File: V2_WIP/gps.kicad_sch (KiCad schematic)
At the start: 38 parts, among them J4 BATT, SW1 RotaryEncoder, SW2 MSN22AFW01, U10 24C32, U101 DFR0654, U2 TPS613222ADBVR

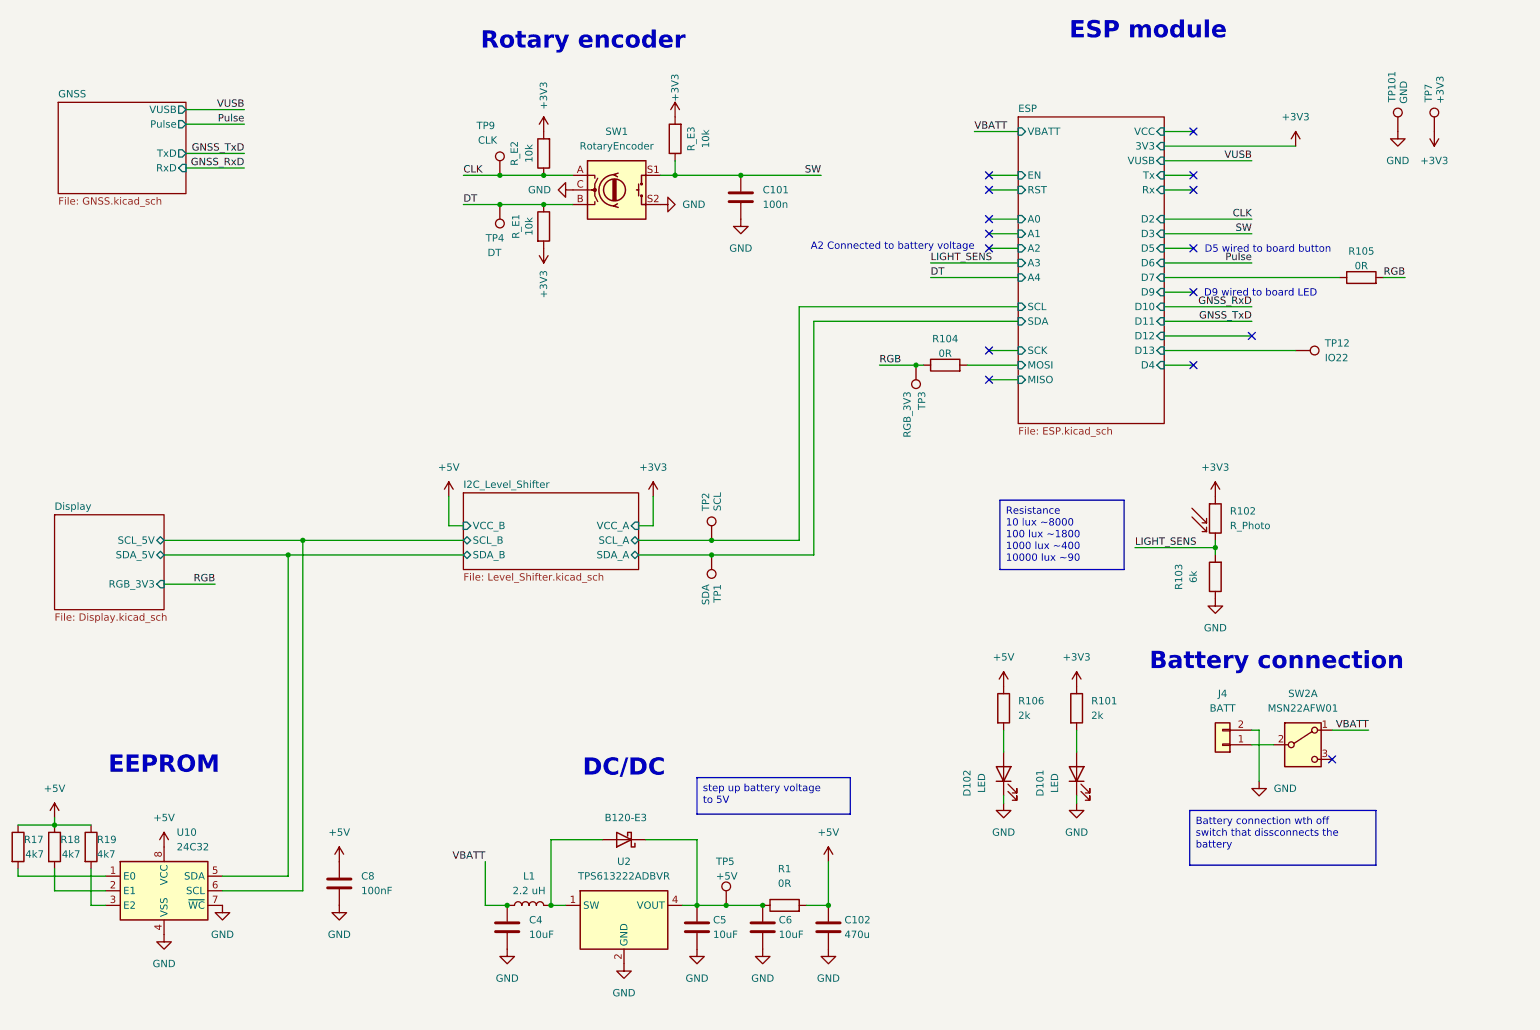
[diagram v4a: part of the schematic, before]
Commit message: added battery monitoring circuits
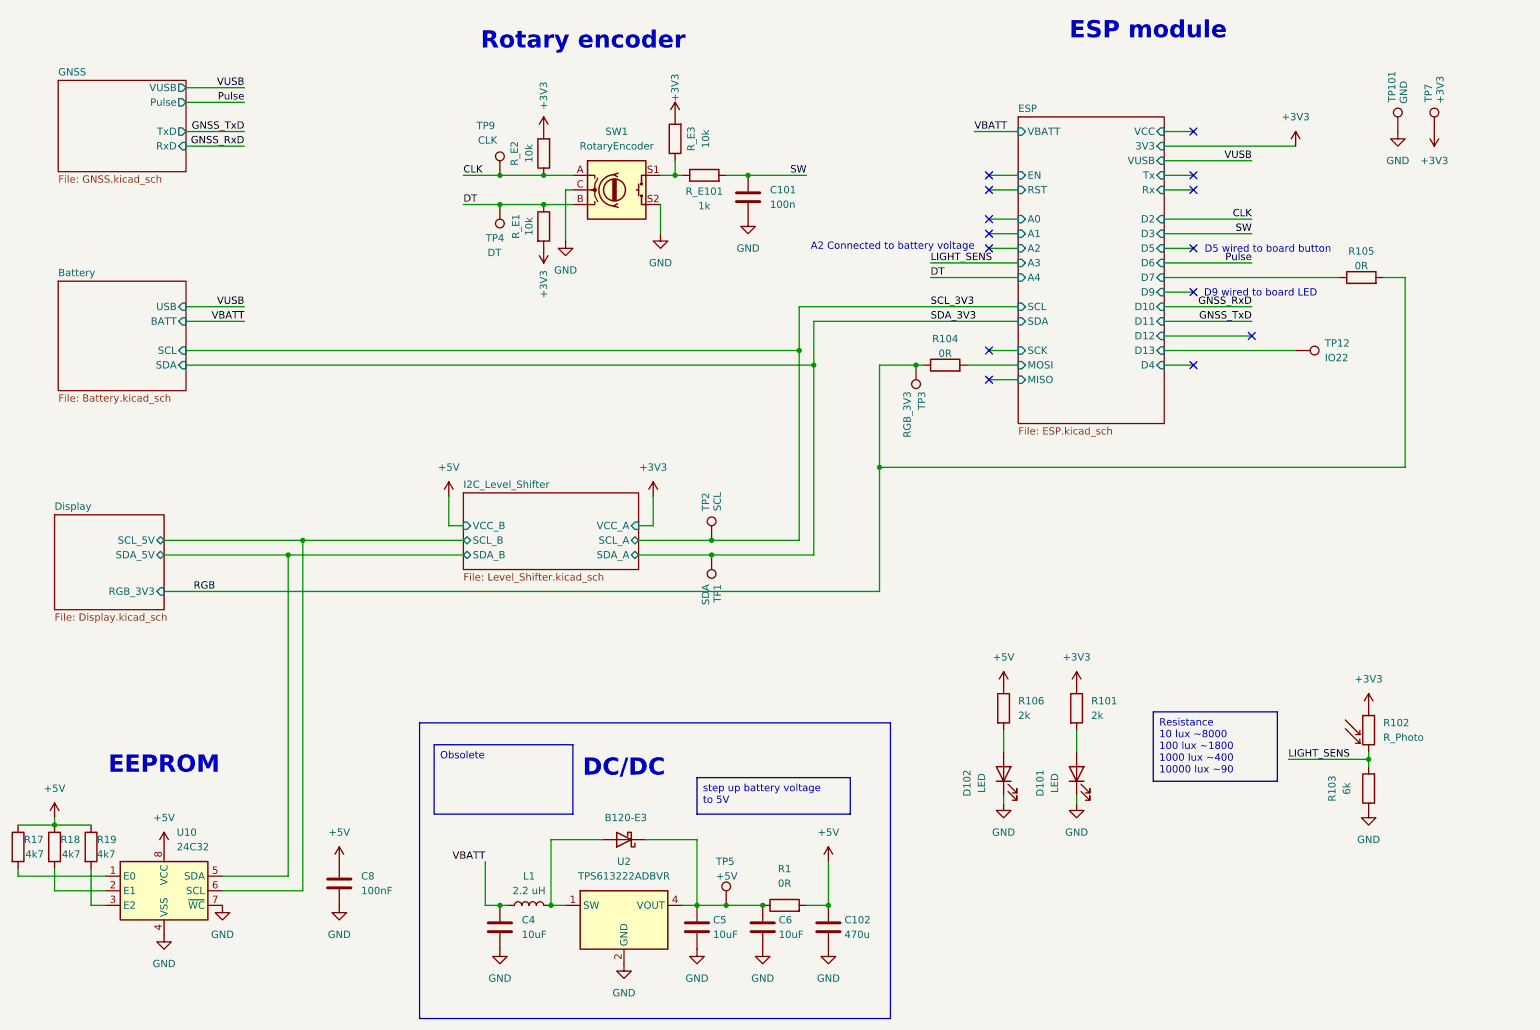
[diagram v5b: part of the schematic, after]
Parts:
- removed J4: BATT, 1769:1769, symbol Connector_Generic:Conn_01x02
- removed SW2: MSN22AFW01, Button_Switch_THT:MSN22AFW01, symbol Switch:SW_DPDT_x2
- added R_E101: 1k, Resistor_SMD:R_0805_2012Metric_Pad1.20x1.40mm_HandSolder, symbol Device:R
- D101, D102: footprint LED_THT:LED_D3.0mm -> Diode_SMD:D_0603_1608Metric_Pad1.05x0.95mm_HandSolder
- R104, R105: footprint Resistor_SMD:R_0805_2012Metric_Pad1.20x1.40mm_HandSolder -> Resistor_SMD:R_0603_1608Metric_Pad0.98x0.95mm_HandSolder
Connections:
- net SW: now also R_E101.2; no longer R_E3.1, SW1.S1
- net ESP/SCL renamed SCL_3V3
- net ESP/SDA renamed SDA_3V3
- new net: R_E101.1, R_E3.1, SW1.S1
- no-connect marks 15 -> 14
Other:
- added sheet Battery (Battery.kicad_sch)
- note removed: "Battery connection"
- moved on the sheet: C101, C4, R102, R103

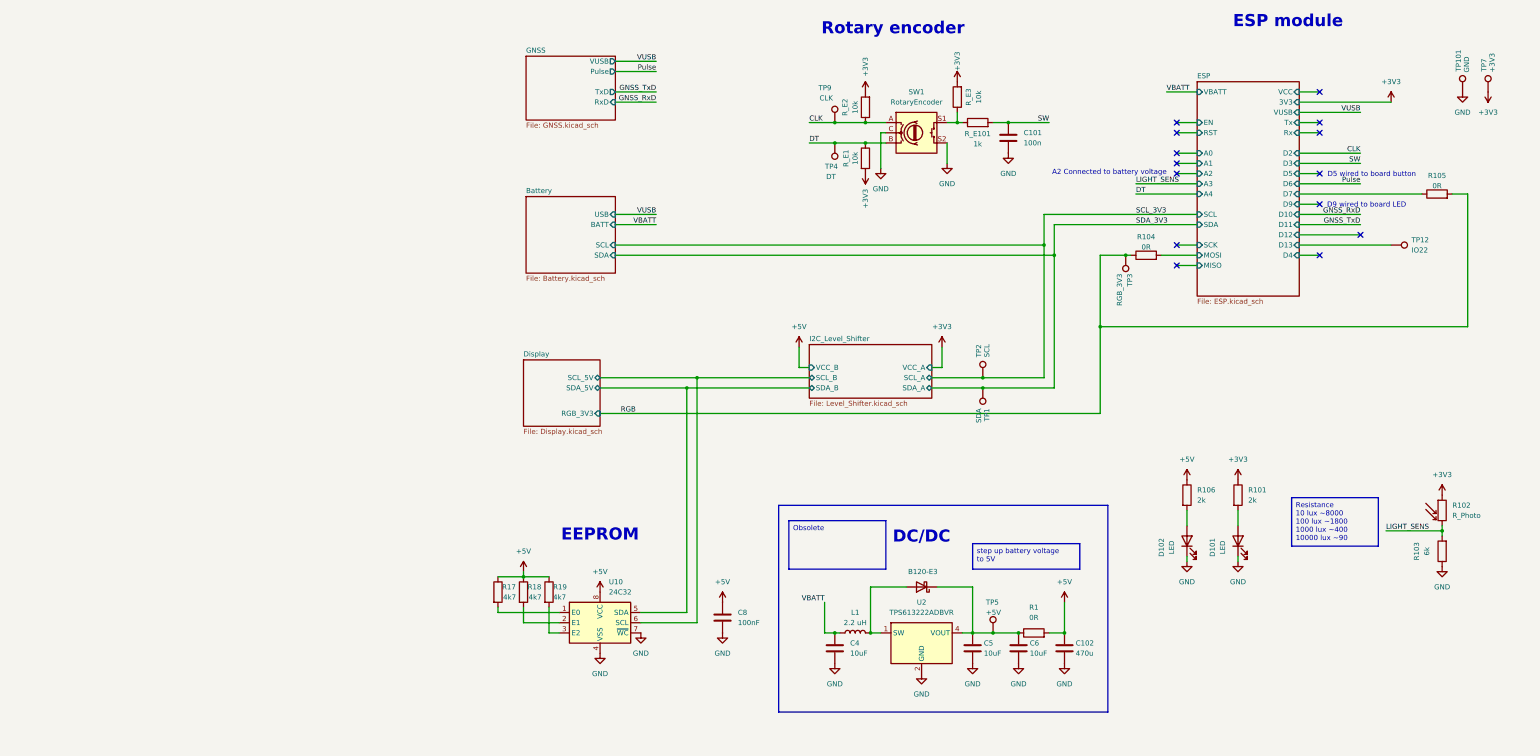
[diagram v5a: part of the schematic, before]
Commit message: added FLASH module; moved encoder into separate schematic
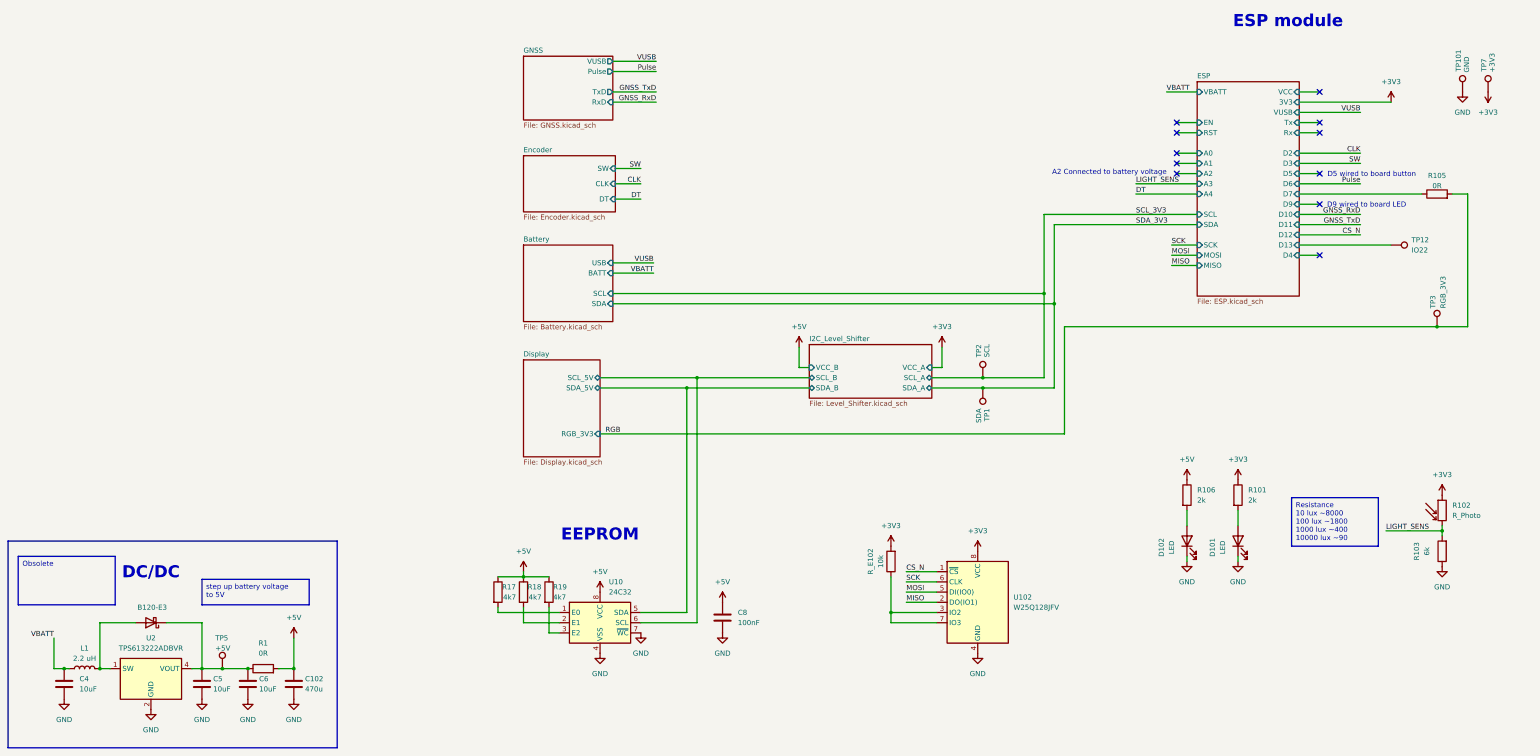
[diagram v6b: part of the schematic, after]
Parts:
- removed C101: 100n, Capacitor_SMD:C_0603_1608Metric_Pad1.08x0.95mm_HandSolder, symbol Device:C
- removed R104: 0R, Resistor_SMD:R_0603_1608Metric_Pad0.98x0.95mm_HandSolder, symbol Device:R
- removed R_E1, R_E2, R_E3: 10k, Resistor_SMD:R_0805_2012Metric_Pad1.20x1.40mm_HandSolder, symbol Device:R
- removed R_E101: 1k, Resistor_SMD:R_0805_2012Metric_Pad1.20x1.40mm_HandSolder, symbol Device:R
- removed SW1: RotaryEncoder, Rotary_Encoder:RotaryEncoder_Alps_EC12E-Switch_Vertical_H20mm_CircularMountingHoles, symbol Device:RotaryEncoder_Switch
- removed TP4: DT, TestPoint:TestPoint_Pad_D1.5mm, symbol Connector:TestPoint
- removed TP9: CLK, TestPoint:TestPoint_Pad_D1.5mm, symbol Connector:TestPoint
- added R_E102: 10k, Resistor_SMD:R_0805_2012Metric_Pad1.20x1.40mm_HandSolder, symbol Device:R
- added U102: W25Q128JFV, Package_SO:SOIC-8_5.23x5.23mm_P1.27mm, symbol Memory_Flash:W25Q128JVS
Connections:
- net +3V3: now also R_E102.2, U102.8 (VCC)
- net GND: now also U102.4 (GND)
- new net: R_E102.1, U102.3 (IO2), U102.7 (IO3)
- new net CS_N: U102.1 (~{CS})
- new net MISO: U102.2 (DO(IO1))
- new net MOSI: U102.5 (DI(IO0))
- new net SCK: U102.6 (CLK)
- no-connect marks 14 -> 11
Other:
- added sheet Encoder (Encoder.kicad_sch)
- note removed: "Rotary encoder"
- moved on the sheet: C102, C4, C5, C6, L1, R1, TP3, TP5, U2

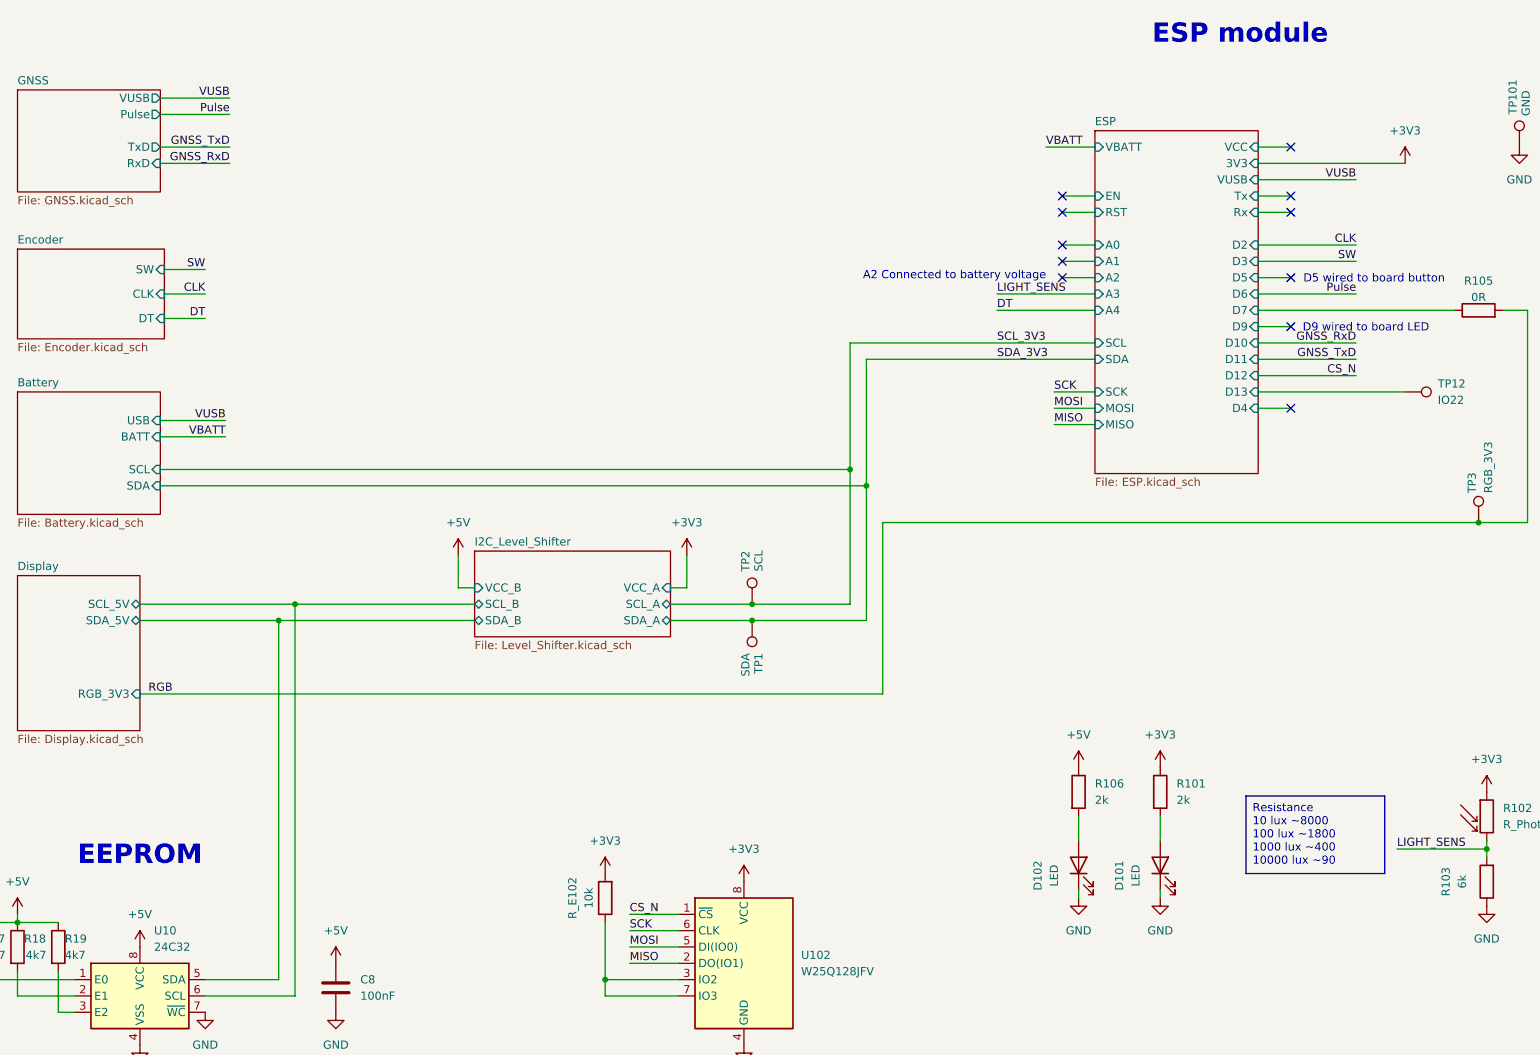
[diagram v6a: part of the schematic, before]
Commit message: added USB, button
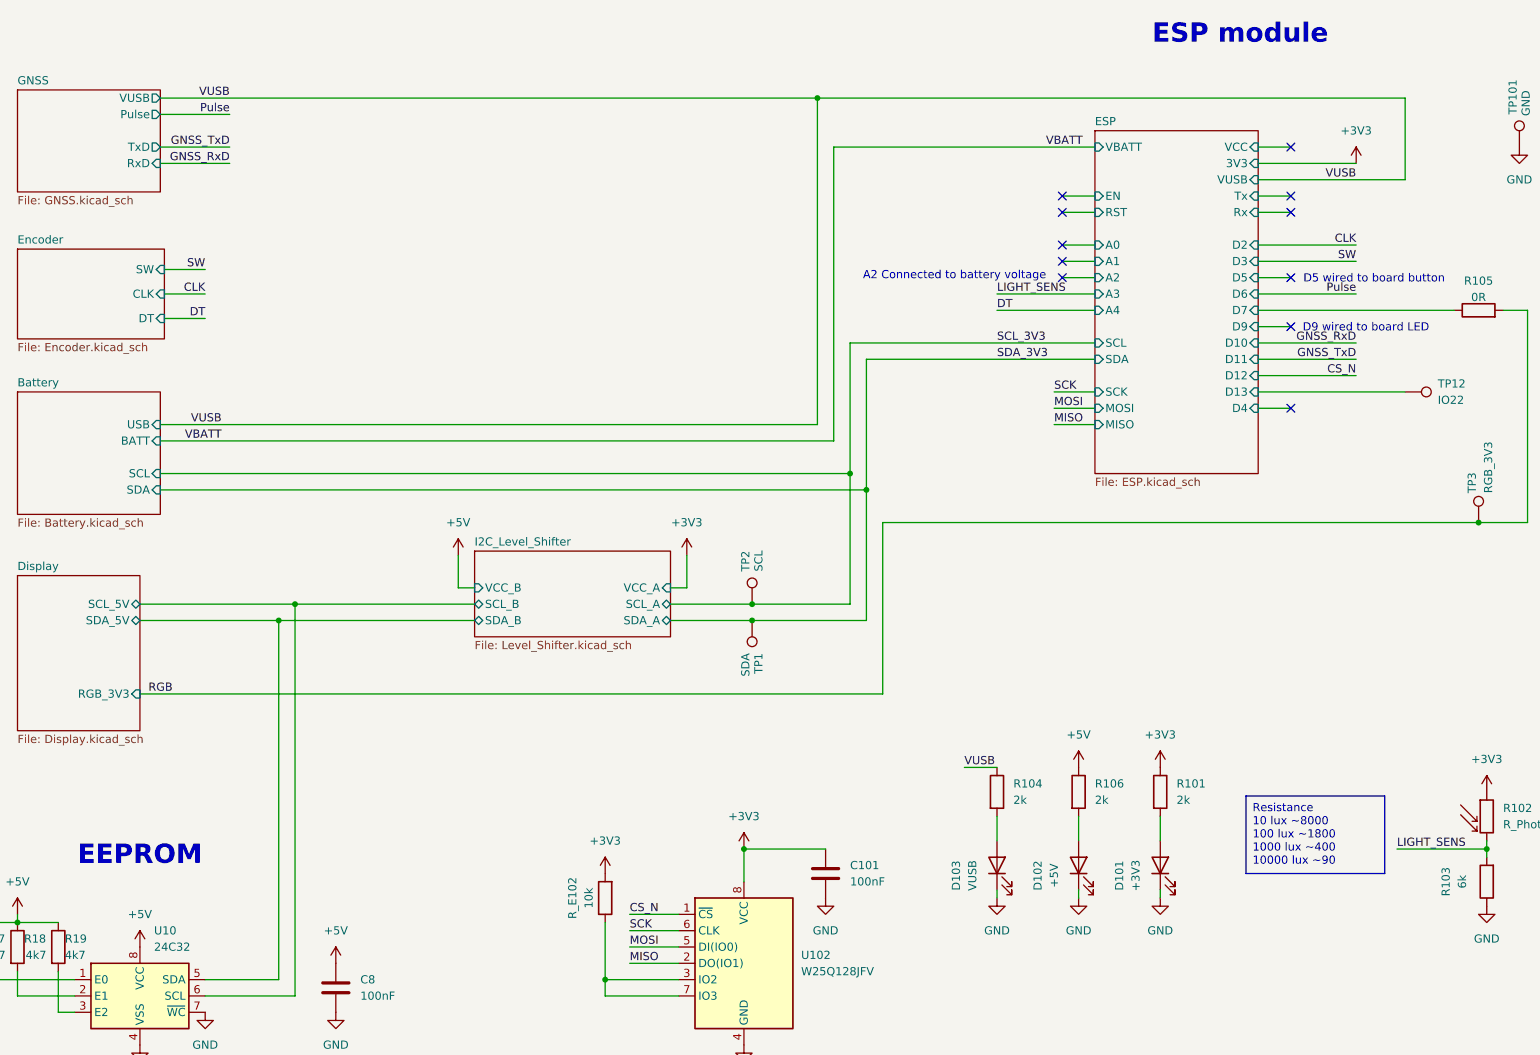
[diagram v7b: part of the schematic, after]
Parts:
- added C101: 100nF, Capacitor_SMD:C_0805_2012Metric_Pad1.18x1.45mm_HandSolder, symbol Device:C
- added D103: VUSB, Diode_SMD:D_0603_1608Metric_Pad1.05x0.95mm_HandSolder, symbol Device:LED
- added R104: 2k, Resistor_SMD:R_0603_1608Metric_Pad0.98x0.95mm_HandSolder, symbol Device:R
- D101: value LED -> +3V3
- D102: value LED -> +5V
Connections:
- net +3V3: now also C101.2
- net GND: now also C101.1, D103.1 (K)
- net VUSB: now also R104.1
- new net: D103.2 (A), R104.2
